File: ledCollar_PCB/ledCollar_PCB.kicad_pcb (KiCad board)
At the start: 2 copper layers, 30 x 20 mm, 26 parts, among them J2 SWD, J3 APA102, J4 MAX9814 Breakout, Q1 AO3400A, SW1 SW_Push, U1 AP2112K-3.3, U2 STM32F103C8Tx, U3 NRF24L01_Breakout, U4 MAX9814

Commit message: some layout tweaks, nothing major
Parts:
- removed J4: MAX9814 Breakout, Connector_PinSocket_2.54mm:PinSocket_1x05_P2.54mm_Vertical
- added C10: 100n, Capacitor_SMD:C_0603_1608Metric, F.Cu at (136.1, 109.5)
- added C11: 10n, Capacitor_SMD:C_0603_1608Metric, F.Cu at (132.1, 109.5)
- added C12: 2n2, Capacitor_SMD:C_0603_1608Metric, F.Cu at (136.1, 107.0)
- added C13: 100n, Capacitor_SMD:C_0603_1608Metric, F.Cu at (132.1, 107.0)
- added U5: MPU-6050, Sensor_Motion:InvenSense_QFN-24_4x4mm_P0.5mm, F.Cu at (126.7, 106.7)
- MK1: footprint Connector_PinHeader_2.54mm:PinHeader_1x02_P2.54mm_Vertical -> LeoDJ:Microphone_9.5mm; moved to B.Cu
- moved C6 42.8 mm to (110.3, 102.3), turned to 180 degrees
- moved C9 40.2 mm to (106.2, 104.6), turned to -90 degrees
- moved R7 39.5 mm to (116.8, 105.4), turned to 90 degrees
- moved R5 38.0 mm to (113.8, 105.4), turned to 90 degrees
- moved U4 36.6 mm to (109.6, 105.0)
- moved R6 36.6 mm to (115.3, 105.4), turned to -90 degrees
- moved C7 34.6 mm to (107.0, 102.3)
- moved C8 33.3 mm to (109.1, 107.6)
- moved C5 28.2 mm to (118.4, 105.4), turned to -90 degrees
- moved MK1 23.2 mm to (116.0, 104.8), turned to 0 degrees
- moved J2 10.9 mm to (128.0, 112.8), turned to 0 degrees
- moved SW1 9.85 mm to (125.2, 103.5)
- moved U3 0.36 mm to (116.2, 113.5)
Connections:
- net Net-(C5-Pad2) renamed /MICIN
- net Net-(R6-Pad2) renamed /MICBIAS
- U2 pad 20: Net-(U2-Pad20) -> MPU_IRQ
- U2 pad 21: Net-(U2-Pad21) -> SCL
- U2 pad 22: Net-(U2-Pad22) -> SDA

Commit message: *layouting sounds*
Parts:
- added J1: PWR+, TestPoint:TestPoint_Pad_1.5x1.5mm, F.Cu at (111.8, 118.0)
- added J2: PWR-, TestPoint:TestPoint_Pad_1.5x1.5mm, F.Cu at (109.2, 118.0)
- added R8: 10k, Resistor_SMD:R_0603_1608Metric, F.Cu at (120.9, 103.1)
- added R9: 10k, Resistor_SMD:R_0603_1608Metric, F.Cu at (119.4, 103.1)
- moved R3 30.1 mm to (110.7, 111.8), turned to 90 degrees
- moved R2 29.4 mm to (110.7, 114.8), turned to 90 degrees
- moved R4 15.0 mm to (124.6, 115.6)
- moved C3 14.4 mm to (118.0, 106.7), turned to 180 degrees
- moved C10 12.4 mm to (124.6, 114.0), turned to 180 degrees
- moved C12 11.8 mm to (124.5, 104.9)
- moved SW1 10.3 mm to (114.9, 103.8)
- moved MK1 8.72 mm to (124.7, 105.1)
- moved C11 8.11 mm to (124.6, 112.5), turned to 180 degrees
- moved C4 5.86 mm to (122.2, 118.9), turned to 180 degrees
- moved U3 5.57 mm to (110.7, 113.7)
- moved J6 5.43 mm to (128.0, 118.2), turned to 180 degrees
- moved C13 4.84 mm to (127.8, 104.9), turned to 180 degrees
- moved C6 4.72 mm to (114.4, 104.5), turned to 0 degrees
- moved C5 3.98 mm to (116.6, 101.8)
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- renumbered J2 to J6
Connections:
- net Net-(J3-Pad1) renamed /LED_GND
- U2 pad 21: SCL -> Net-(U2-Pad21)
- U2 pad 22: SDA -> Net-(U2-Pad22)
- U2 pad 45: Net-(U2-Pad45) -> SCL
- U2 pad 46: Net-(U2-Pad46) -> SDA
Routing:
- net +3V3: track 0.00 -> 94.9 mm, vias 0 -> 8
- net GND: track 0.00 -> 70.9 mm, vias 0 -> 19
- net SPI2_COPI: track 0.00 -> 28.7 mm, vias 0 -> 2
- net SPI2_SCK: track 0.00 -> 24.1 mm, vias 0 -> 2
- net VCC: track 0.00 -> 22.9 mm
- net MPU_IRQ: track 0.00 -> 19.5 mm, vias 0 -> 2
- net SWDIO: track 0.00 -> 17.5 mm
- net LED_ENABLE: track 0.00 -> 17.1 mm
- net NRF_IRQ: track 0.00 -> 15.2 mm, vias 0 -> 1
- net SCL: track 0.00 -> 12.6 mm, vias 0 -> 2
- net SDA: track 0.00 -> 11.2 mm
- net MIC_OUT: track 0.00 -> 11.0 mm, vias 0 -> 2
- net SWCLK: track 0.00 -> 9.35 mm
- net Net-(C5-Pad1): track 0.00 -> 9.24 mm
- net /MICIN: track 0.00 -> 8.87 mm
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- added copper zone on B.Cu, net GND
- added copper zone on F.Cu, net GND
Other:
- board text added: "+"
- board text added: "-"
- board text added: "VCC DATA CLK GND"

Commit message: add light sensor
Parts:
- added Q2: Q_Photo_NPN, LED_SMD:LED_0805_2012Metric_Castellated, B.Cu at (103.2, 104.2)
- added R10: 10k, Resistor_SMD:R_0603_1608Metric, F.Cu at (103.2, 102.2)
- moved Q1 1.66 mm to (103.8, 116.1)
- moved R1 1.64 mm to (103.8, 118.7)
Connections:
- U2 pad 17: Net-(U2-Pad17) -> MIC_OUT
- U2 pad 18: MIC_OUT -> LIGHT_SENSE
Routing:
- net LIGHT_SENSE: track 0.00 -> 21.5 mm, vias 0 -> 3
- net +3V3: track 94.9 -> 97.4 mm, vias 8 -> 9
- net GND: track 70.9 -> 72.6 mm
- net LED_ENABLE: track 17.1 -> 15.6 mm
- net /LED_GND: track 2.85 -> 3.42 mm
- net MIC_OUT: track 11.0 -> 10.5 mm
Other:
- board text added: "D C G"

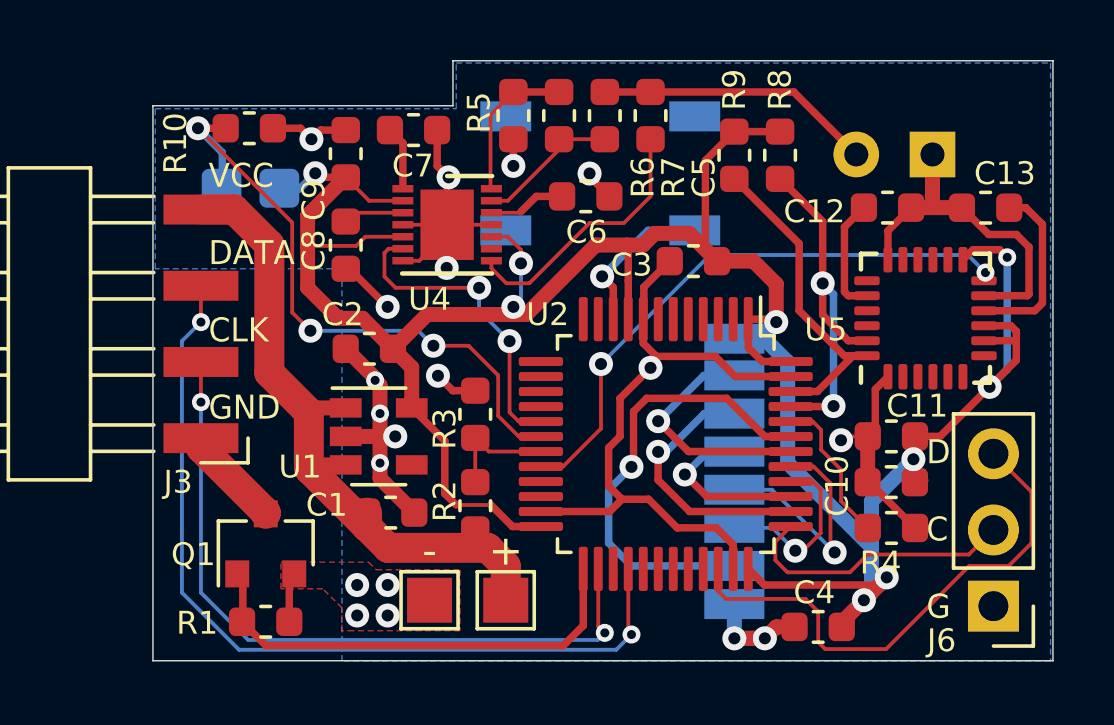
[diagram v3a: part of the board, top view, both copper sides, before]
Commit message: add alternate NRF footprint
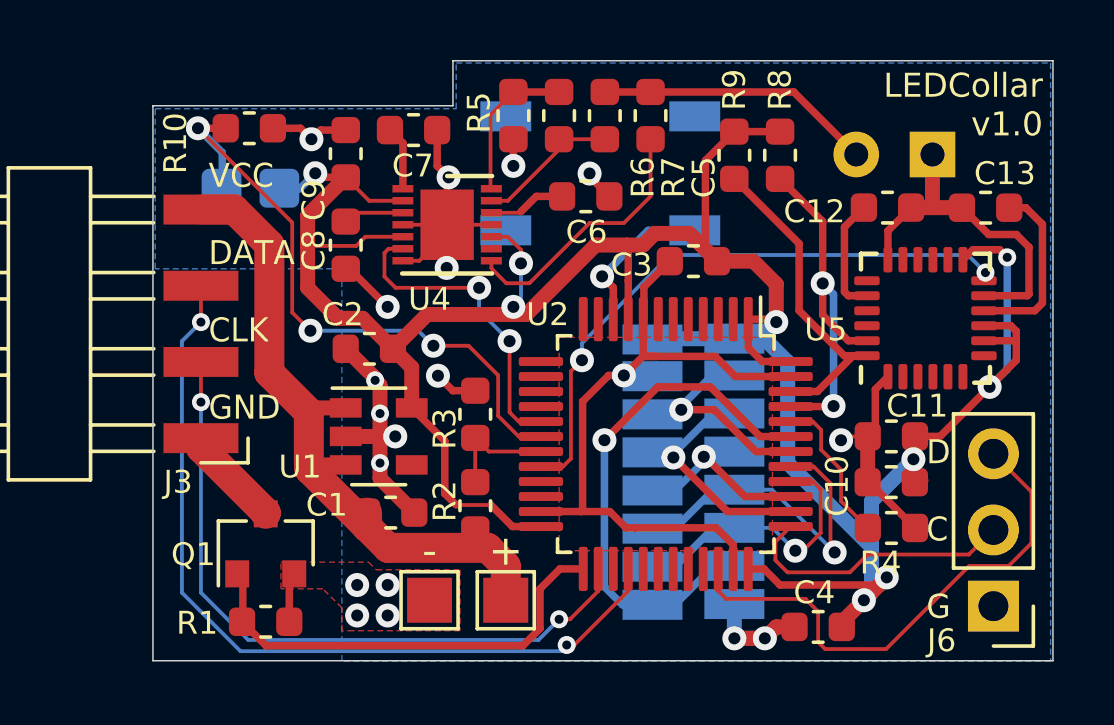
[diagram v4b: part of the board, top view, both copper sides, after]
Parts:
- added U6: NRF24L01_Breakout, LeoDJ:NRF24L01_SMD_PadsOnly, B.Cu at (108.0, 113.7)
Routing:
- net SPI1_COPI: track 8.13 -> 11.4 mm
- net SPI1_CIPO: track 6.00 -> 9.27 mm
- net +3V3: track 97.4 -> 100.2 mm
- net NRF_IRQ: track 15.2 -> 17.6 mm
- net SPI1_SCK: track 5.80 -> 7.80 mm
- net SPI2_SCK: track 24.1 -> 23.0 mm
- net GND: track 72.6 -> 73.7 mm
- net SPI2_COPI: track 28.7 -> 27.7 mm
- net MPU_IRQ: track 19.5 -> 20.3 mm
- net NRF_CE: track 8.01 -> 8.51 mm
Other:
- board text added: "LEDCollar v1.0"

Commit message: PCB finishing touches
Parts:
- added GR1: QR Code, LeoDJ:QR_Code_LEDCollar, B.Cu at (108.0, 104.1)
- added GR2: Logo_Open_Hardware_Small, Symbol:OSHW-Logo2_7.3x6mm_SilkScreen, B.Cu at (123.7, 114.7)
- J3: footprint Connector_Harwin:Harwin_M20-89004xx_1x04_P2.54mm_Horizontal -> LeoDJ:APA102_SolderPads
- moved J3 5.40 mm to (101.5, 108.8), turned to 90 degrees
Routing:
- net GND: track 73.7 -> 74.4 mm, vias 19 -> 20
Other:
- outline, holes or cut-outs redrawn
- board text added: "LEDCollar"
- board text added: "SWD"
- board text added: "https://github.com /LeoDJ/ledCollar"
- board text added: "v1.0"
- board text removed: "LEDCollar v1.0"

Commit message: add cap to STM32 reset pin
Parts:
- added C14: 100n, Capacitor_SMD:C_0603_1608Metric, F.Cu at (119.3, 106.7)
- Q2: value Q_Photo_NPN -> Senba SMD0805-20
- moved C3 1.30 mm to (117.0, 105.9), turned to -90 degrees
- moved GR1 0.18 mm to (108.0, 104.3)
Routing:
- net GND: track 74.4 -> 77.9 mm
- net Net-(C14-Pad2): track 0.00 -> 2.93 mm
- net +3V3: track 100.2 -> 101.2 mm, vias 9 -> 10

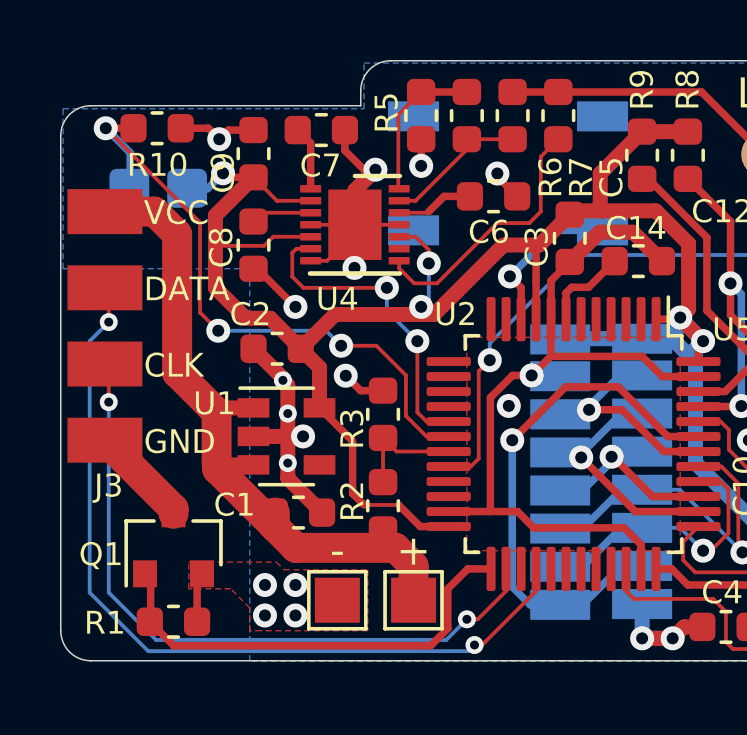
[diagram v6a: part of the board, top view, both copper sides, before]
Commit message: add ADC input bypass caps
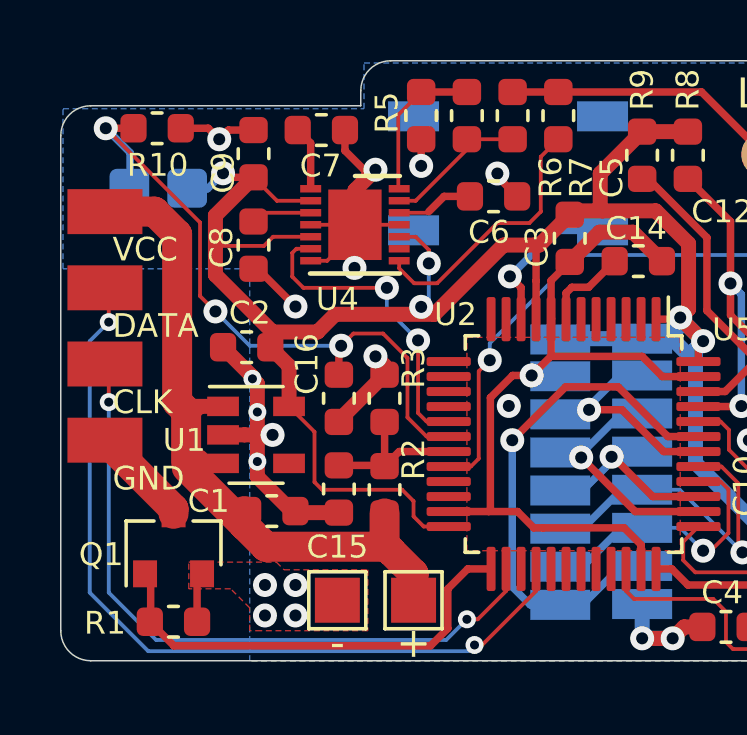
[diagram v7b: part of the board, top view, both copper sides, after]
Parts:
- added C15: 100n, Capacitor_SMD:C_0603_1608Metric, F.Cu at (109.3, 114.3)
- added C16: 100n, Capacitor_SMD:C_0603_1608Metric, F.Cu at (109.3, 111.3)
- moved U1 1.02 mm to (106.5, 112.5)
- moved C2 1.02 mm to (106.2, 109.5)
- moved C1 0.89 mm to (107.0, 115.0)
- moved R3 0.54 mm to (110.8, 111.3)
- moved R2 0.54 mm to (110.8, 114.3)
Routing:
- net GND: track 77.9 -> 80.9 mm
- net VCC: track 23.1 -> 24.8 mm
- net V_SENSE: track 3.85 -> 5.35 mm
- net LIGHT_SENSE: track 21.5 -> 22.9 mm
- net +3V3: track 101.2 -> 102.3 mm

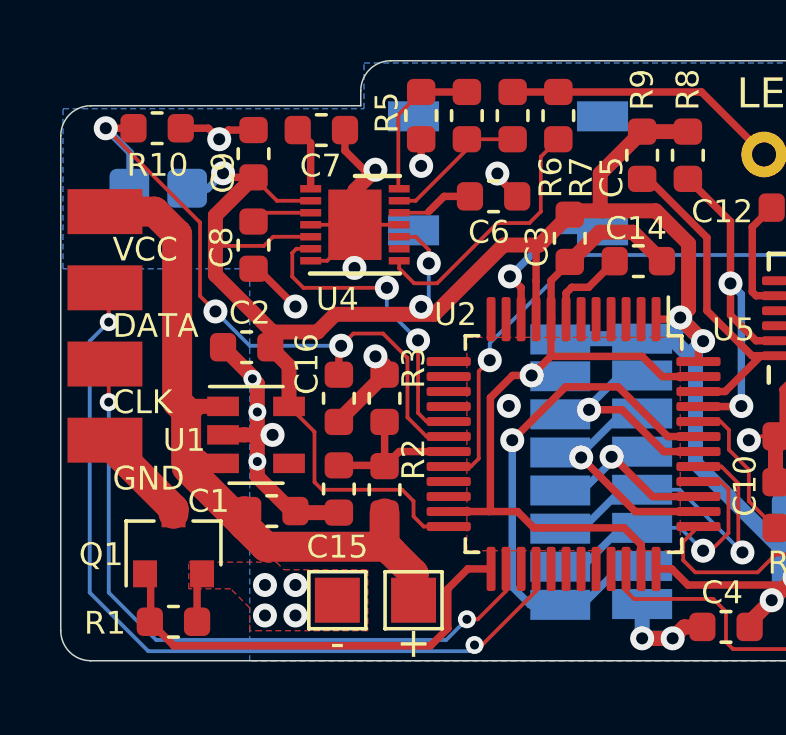
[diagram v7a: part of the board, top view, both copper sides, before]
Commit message: fix quiescent current of MAX9814 and voltage dividers
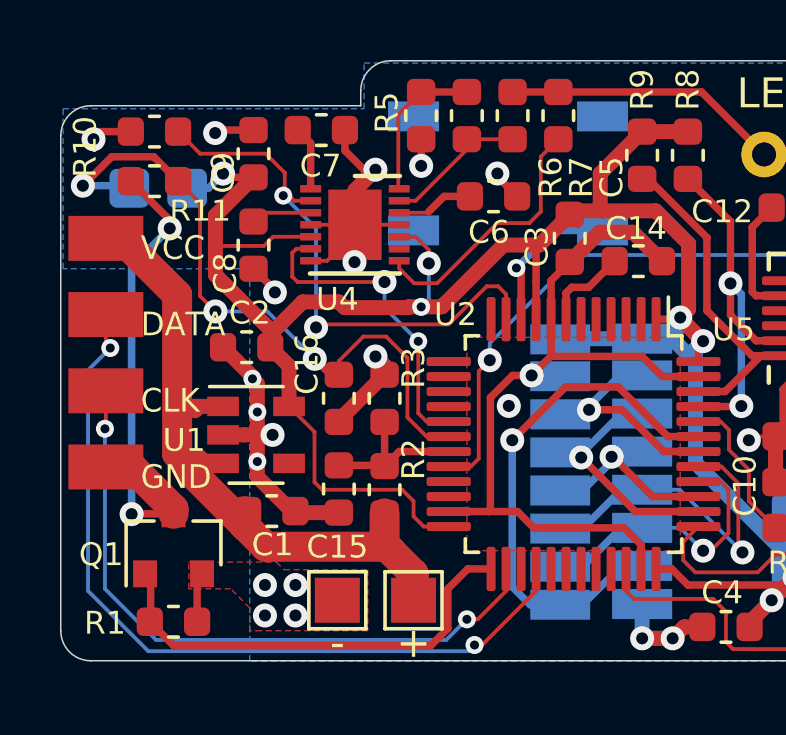
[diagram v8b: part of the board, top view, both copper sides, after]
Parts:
- added R11: 10k, Resistor_SMD:R_0603_1608Metric, F.Cu at (103.1, 102.4)
- moved R10 1.77 mm to (103.1, 104.0), turned to 180 degrees
- moved J3 0.89 mm to (101.5, 109.7)
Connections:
- J3 pad 1: /LED_GND -> LED_GND
- Q1 pad 3: /LED_GND -> LED_GND
- R10 pad 2: GND -> LED_GND
- U2 pad 11: Net-(U2-Pad11) -> MIC_ENABLE
- U4 pad 2: +3V3 -> MIC_ENABLE
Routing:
- net MIC_ENABLE: track 0.00 -> 18.6 mm, vias 0 -> 2
- net LED_GND: track 0.00 -> 16.6 mm, vias 0 -> 2
- net /LED_GND: track 3.40 -> 0.00 mm
- net +3V3: track 102.3 -> 100.0 mm
- net VCC: track 24.8 -> 23.3 mm
- net GND: track 80.9 -> 79.9 mm, vias 20 -> 21
- net SPI2_SCK: track 23.0 -> 22.1 mm
- net SPI2_COPI: track 27.7 -> 26.9 mm
- net LIGHT_SENSE: track 22.9 -> 22.4 mm
